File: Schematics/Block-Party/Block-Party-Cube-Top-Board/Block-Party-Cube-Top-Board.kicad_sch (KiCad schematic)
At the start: 5 parts

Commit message: Revision 1.01 of the PCBs
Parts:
- removed J2, J3, J4, J5: ~, Connector_PinHeader_2.54mm:PinHeader_1x01_P2.54mm_Vertical, symbol Quinn_lib:HDR-M-2.54_1x1
- added J2: 4328, adafruit-jst-4328:ADAFRUIT_4328, symbol 4328:4328
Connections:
- net +5V: now also J2.4
- net GND: now also J2.1, J2.SH1 (SHIELD), J2.SH2 (SHIELD)
- net at J1.2 (SIG): now also J2.2
- net at J1.3 (DOUT): now also J2.3

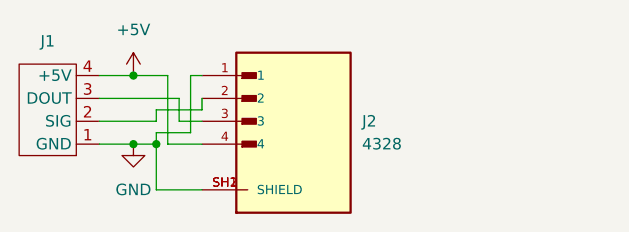
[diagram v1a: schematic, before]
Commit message: Found a good jst part number and updated the BOMs
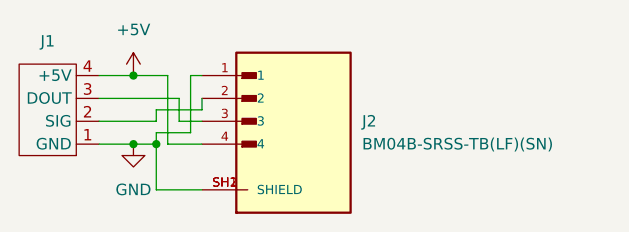
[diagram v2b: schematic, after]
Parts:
- J2: value 4328 -> BM04B-SRSS-TB(LF)(SN); MANUFACTURER Adafruit -> JST
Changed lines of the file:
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@@
 			)
 		)
-		(property "Value" "4328"
+		(property "Value" "BM04B-SRSS-TB(LF)(SN) "
 			(at 181.61 83.8199 0)
 			(effects
@@
 			)
 		)
-		(property "Description" ""
+		(property "Description" "BM04B-SRSS-TB(LF)(SN) "
 			(at 173.99 83.82 0)
 			(effects
@@
 			)
 		)
-		(property "MANUFACTURER" "Adafruit"
+		(property "MANUFACTURER" "JST"
 			(at 173.99 83.82 0)
 			(effects
